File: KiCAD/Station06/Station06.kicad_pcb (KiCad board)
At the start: 2 copper layers, 11 parts, among them J1 LSHM-120-02.5-L-DV-A-S-TR, J10 CONSMA001-SMD-G, J11 CONSMA001-SMD-G, J2 CONSMA001-SMD-G, J3 CONSMA001-SMD-G, J4 CONSMA001-SMD-G, J5 CONSMA001-SMD-G, J6 CONSMA001-SMD-G, J7 CONSMA001-SMD-G, J8 CONSMA001-SMD-G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

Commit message: more work on Station06
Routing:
- net Net-(J1-Pad22): track 0.00 -> 39.4 mm, vias 0 -> 2
- net Net-(J1-Pad18): track 0.00 -> 39.3 mm, vias 0 -> 2
- net Net-(J1-Pad26): track 0.00 -> 38.8 mm, vias 0 -> 2
- net Net-(J1-Pad14): track 0.00 -> 38.6 mm, vias 0 -> 2
- net Net-(J1-Pad30): track 0.00 -> 37.6 mm, vias 0 -> 2
- net Net-(J1-Pad10): track 0.00 -> 37.2 mm, vias 0 -> 2
- net Net-(J1-Pad34): track 0.00 -> 36.1 mm, vias 0 -> 2
- net Net-(J1-Pad6): track 0.00 -> 35.7 mm, vias 0 -> 2
- net Net-(J1-Pad38): track 0.00 -> 34.2 mm, vias 0 -> 2
- net Net-(J1-Pad2): track 0.00 -> 33.7 mm, vias 0 -> 2
- net GND: track 0.00 -> 20.7 mm, vias 0 -> 40
- added copper zone on B.Cu, net GND
- added copper zone on F.Cu, net GND
- added copper zone on In2.Cu, net GND
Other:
- board outline added: 84.3 x 50.8 mm
- copper layers 2 -> 4
- net class Ground added: clearance 0.2, trace_width 0.25, via_dia 1.27, via_drill 1.016

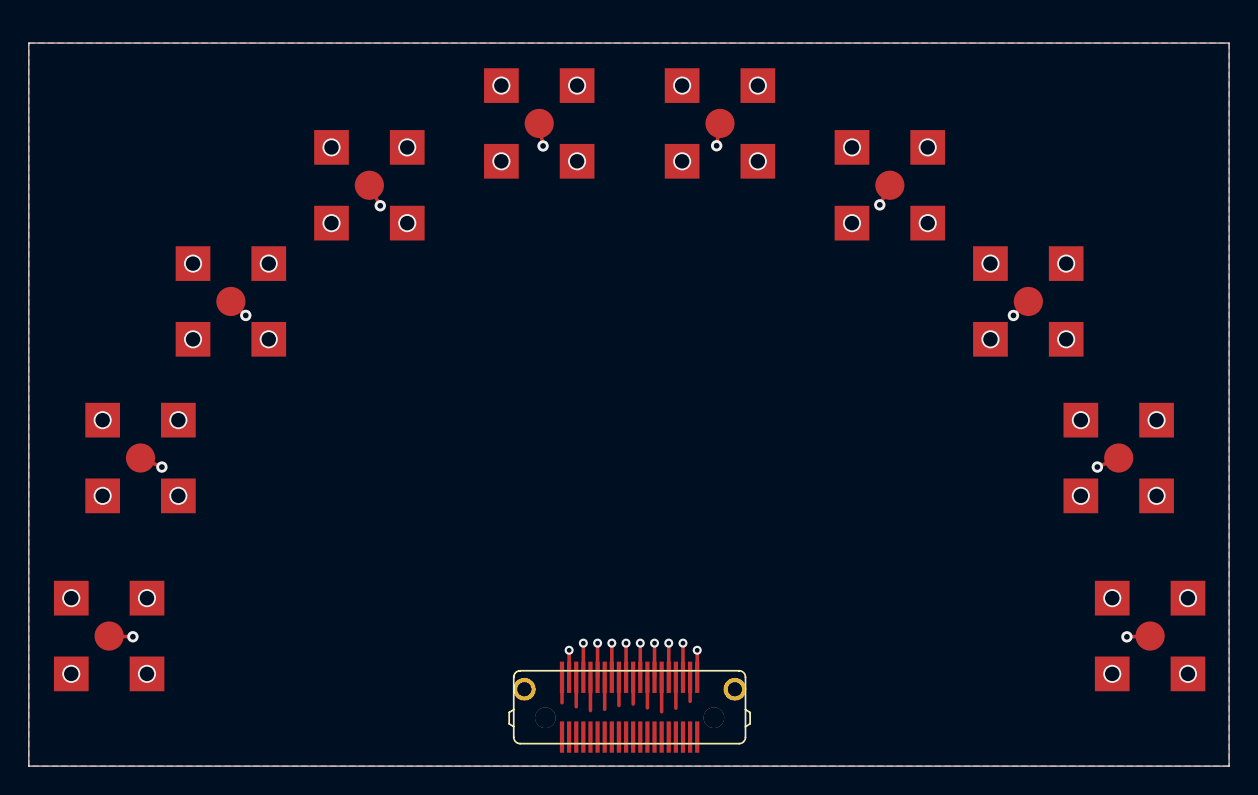
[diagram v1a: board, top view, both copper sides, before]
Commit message: finished Station06
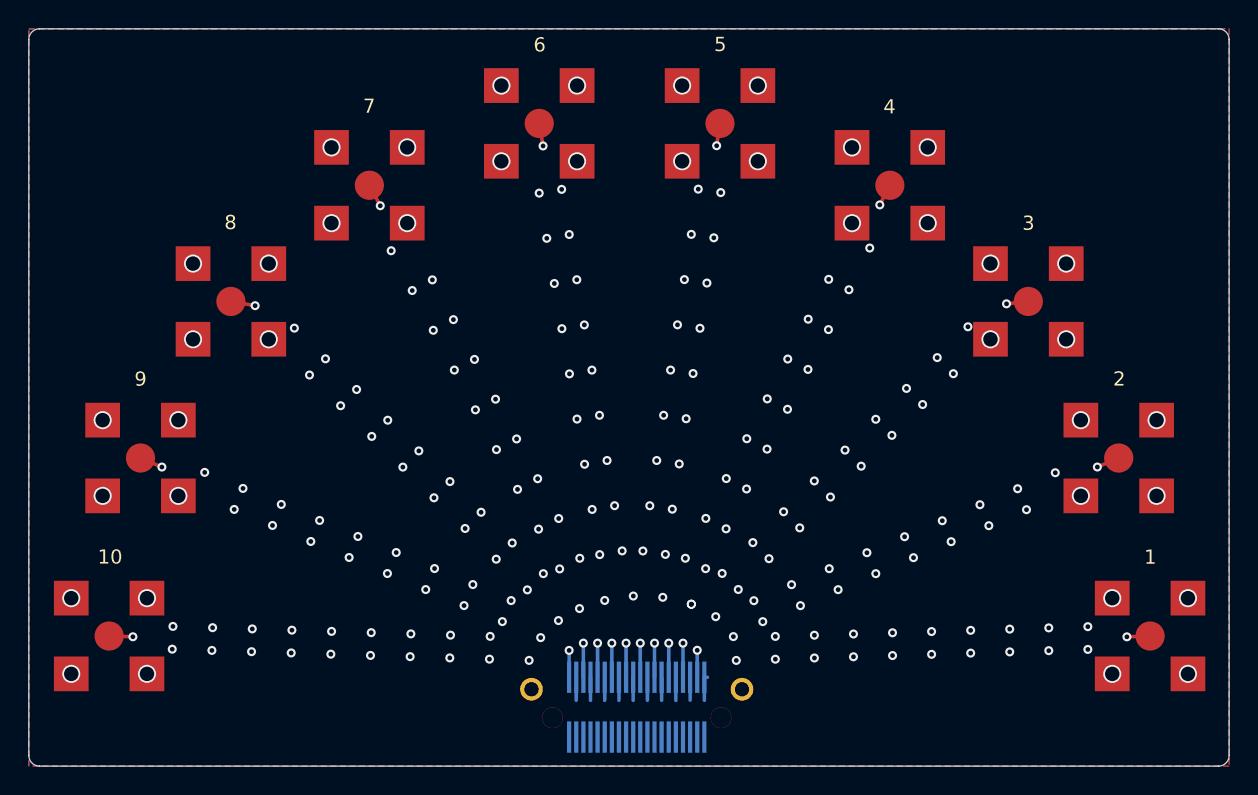
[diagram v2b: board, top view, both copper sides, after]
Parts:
- J1: moved to B.Cu
- moved J1 0.50 mm to (140.5, 100.0), turned to 180 degrees
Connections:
- J10 pad 1: Net-(J1-Pad34) -> Net-(J1-Pad6)
- J11 pad 1: Net-(J1-Pad38) -> Net-(J1-Pad2)
- J2 pad 1: Net-(J1-Pad2) -> Net-(J1-Pad38)
- J3 pad 1: Net-(J1-Pad6) -> Net-(J1-Pad34)
- J4 pad 1: Net-(J1-Pad10) -> Net-(J1-Pad30)
- J5 pad 1: Net-(J1-Pad14) -> Net-(J1-Pad26)
- J6 pad 1: Net-(J1-Pad18) -> Net-(J1-Pad22)
- J7 pad 1: Net-(J1-Pad22) -> Net-(J1-Pad18)
- J8 pad 1: Net-(J1-Pad26) -> Net-(J1-Pad14)
- J9 pad 1: Net-(J1-Pad30) -> Net-(J1-Pad10)
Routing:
- net GND: track 20.7 -> 16.4 mm, vias 40 -> 226
- net Net-(J1-Pad10): track 37.2 -> 37.9 mm
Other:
- board size 84.3 x 50.8 mm -> 84.3 x 51.8 mm
- board text added: "1"
- board text added: "10"
- board text added: "2"
- board text added: "3"
- board text added: "4"
- board text added: "5"
- board text added: "6"
- board text added: "7"
- board text added: "8"
- board text added: "9"
- board text added: "Dylan Oh Jan 2020"
- board text added: "Station06"

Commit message: added via border to Station06 and finalised
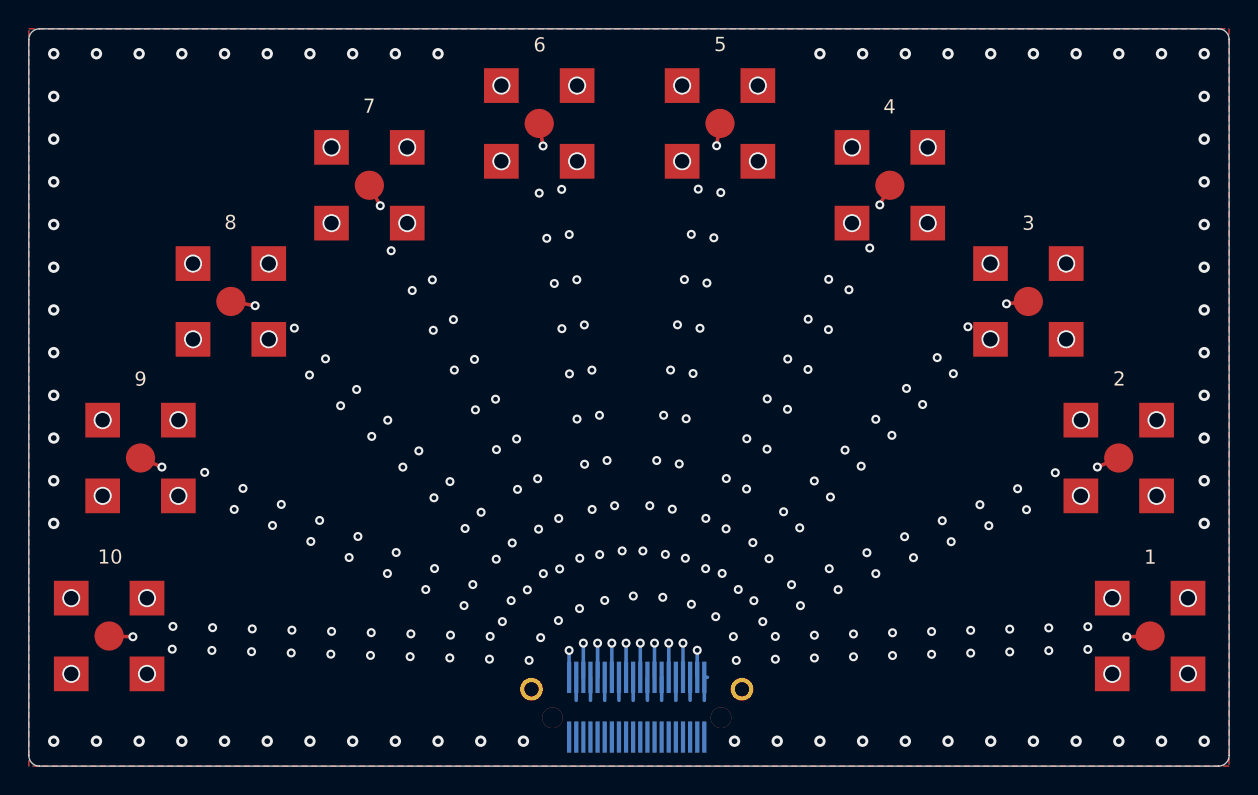
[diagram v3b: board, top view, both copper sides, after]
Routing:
- net GND: vias 226 -> 291
